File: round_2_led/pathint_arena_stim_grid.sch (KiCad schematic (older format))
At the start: 10 parts, among them J1 conn_2x13_odd_even

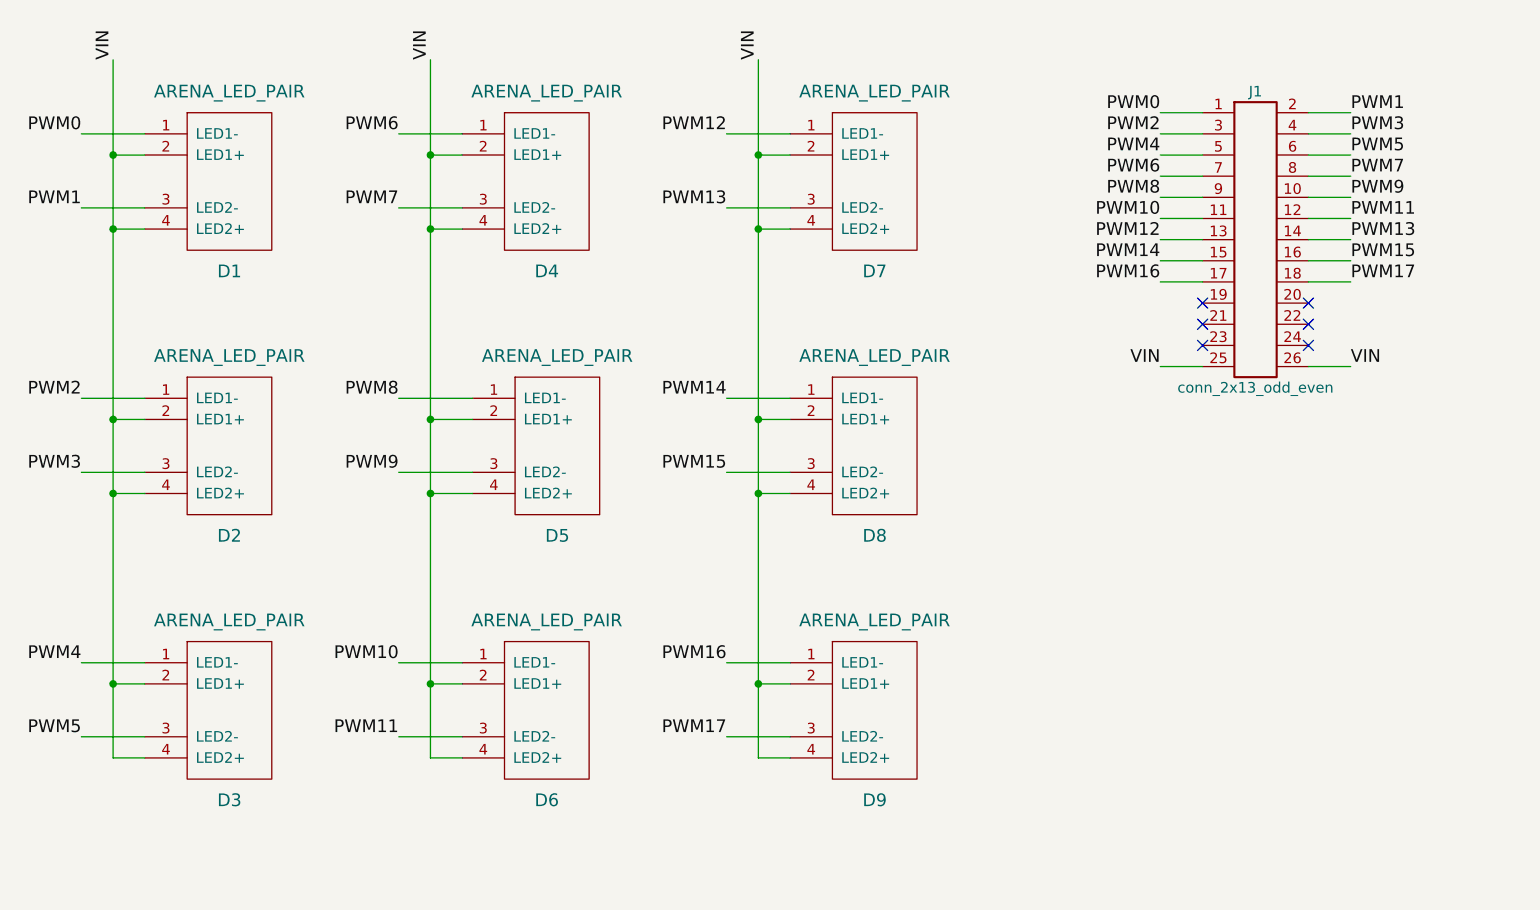
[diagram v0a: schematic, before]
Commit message: Added new design w/ circular arenas and leds at 60 degree angle.
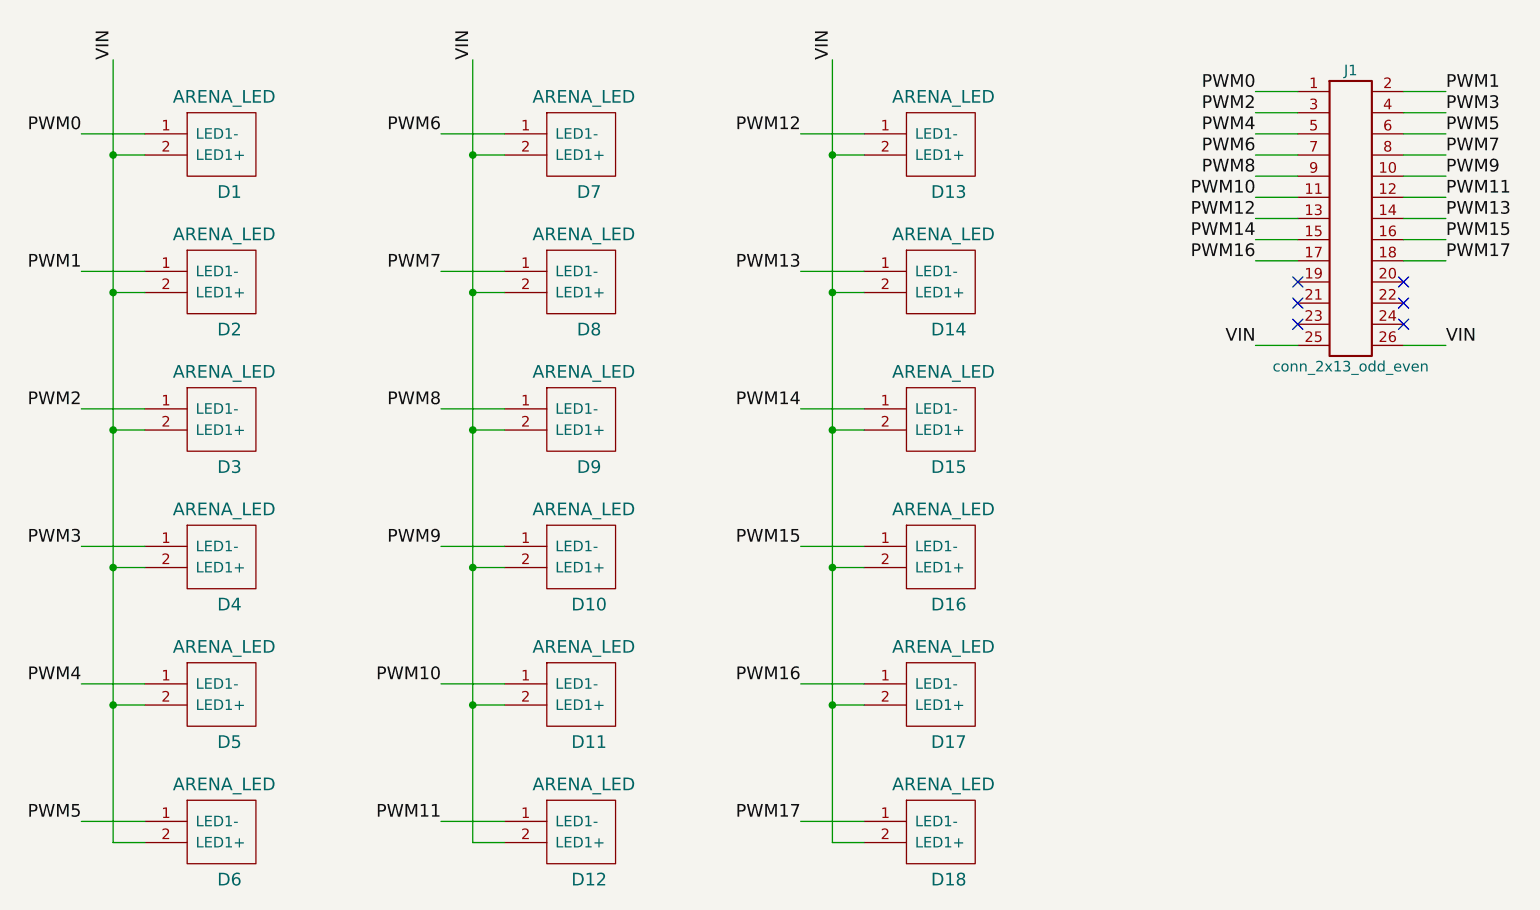
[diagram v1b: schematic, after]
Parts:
- removed D1, D2, D3, D4, D5, D6, D7, D8, D9: ARENA_LED_PAIR, ARENA_ELEM:SUB_ARENA, symbol ARENA_LED_PAIR
- added D1, D10, D11, D12, D13, D14, D15, D16, D17, D18, D2, D3, D4, D5, D6, D7, D8, D9: ARENA_LED, ARENA_ELEM:SUB_ARENA, symbol ARENA_LED
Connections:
- net PWM0: now also D1.1 (LED1-)
- net PWM1: now also D2.1 (LED1-)
- net PWM10: now also D11.1 (LED1-)
- net PWM11: now also D12.1 (LED1-)
- net PWM12: now also D13.1 (LED1-)
- net PWM13: now also D14.1 (LED1-)
- net PWM14: now also D15.1 (LED1-)
- net PWM15: now also D16.1 (LED1-)
- net PWM16: now also D17.1 (LED1-)
- net PWM17: now also D18.1 (LED1-)
- net PWM2: now also D3.1 (LED1-)
- net PWM3: now also D4.1 (LED1-)
- net PWM4: now also D5.1 (LED1-)
- net PWM5: now also D6.1 (LED1-)
- net PWM6: now also D7.1 (LED1-)
- net PWM7: now also D8.1 (LED1-)
- net PWM8: now also D9.1 (LED1-)
- net PWM9: now also D10.1 (LED1-)
- net VIN: now also D1.2 (LED1+), D10.2 (LED1+), D11.2 (LED1+), D12.2 (LED1+), D13.2 (LED1+), D14.2 (LED1+), D15.2 (LED1+), D16.2 (LED1+), D17.2 (LED1+), D18.2 (LED1+), D2.2 (LED1+), D3.2 (LED1+), D4.2 (LED1+), D5.2 (LED1+), D6.2 (LED1+), D7.2 (LED1+), D8.2 (LED1+), D9.2 (LED1+)
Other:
- moved on the sheet: J1
